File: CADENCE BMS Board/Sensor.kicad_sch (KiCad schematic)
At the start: 65 parts, among them IC1 R5432V407BA, J1 Screw_Terminal_01x02, J21 Conn_01x02, Q1 P-Channel FET, Q10 N-MOS, Q2 60V Enhancement, Q3 60V Enhancement, Q4 60V Enhancement, Q5 Q_NMOS_DSG, Q6 Q_NMOS_DSG, Q7 Q_NMOS_DSG, Q8 N-MOS, Q9 N-MOS, U4 BQ34Z100-R2, U5 MCP9600-E_MX

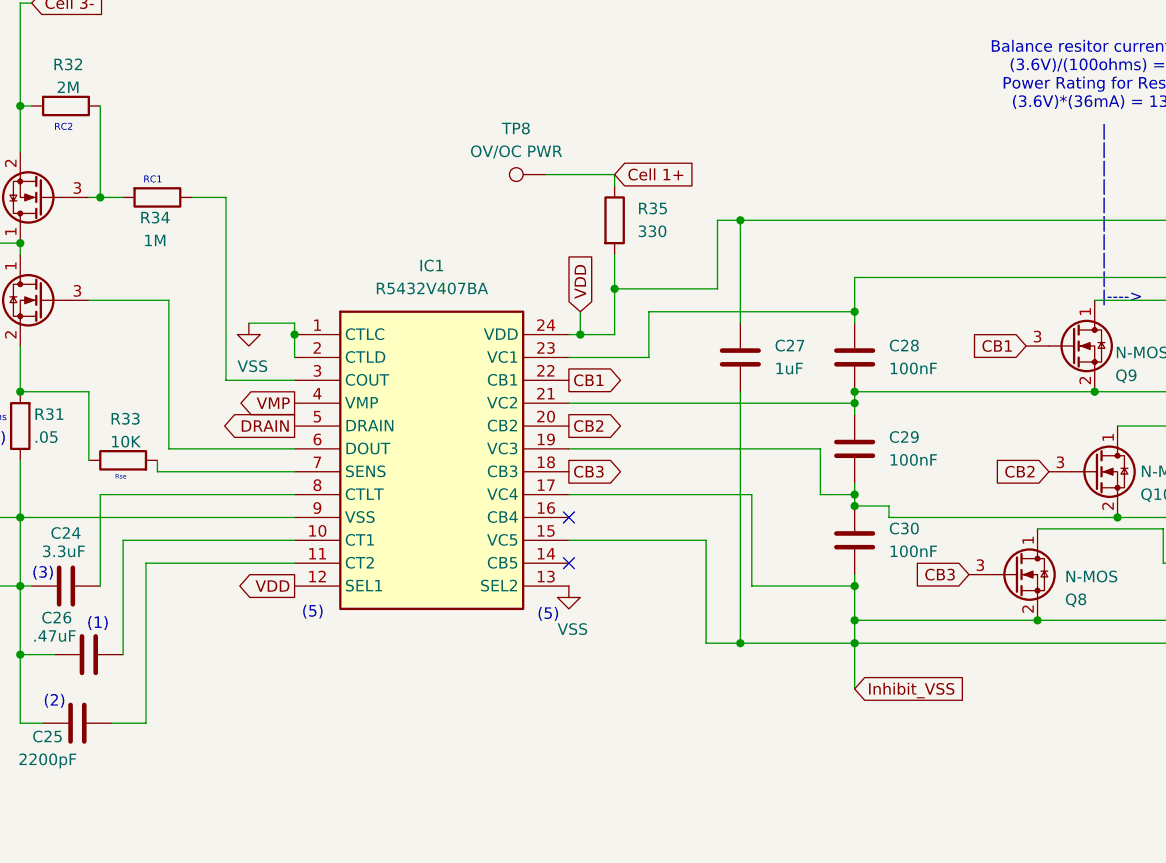
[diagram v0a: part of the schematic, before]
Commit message: Updates to the Inhibit system and Connectors
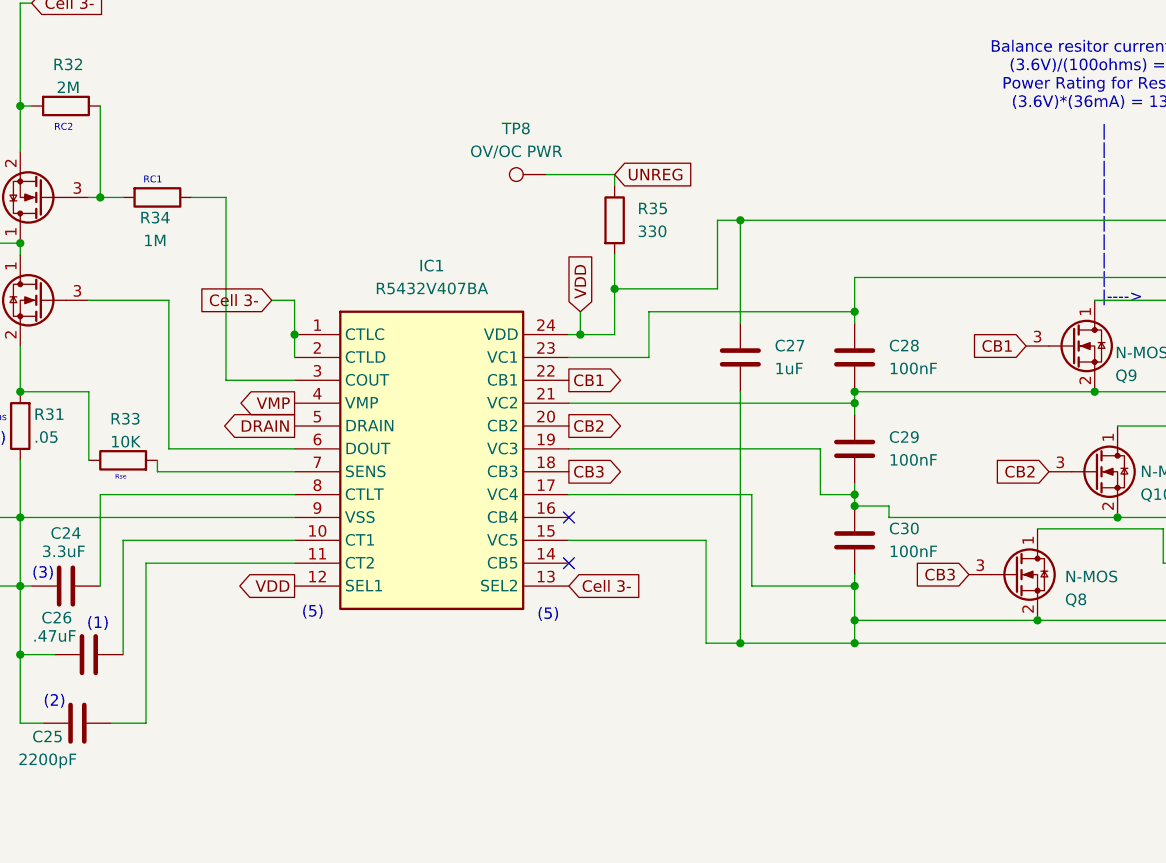
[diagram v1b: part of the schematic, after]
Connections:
- net Cell 1+: no longer R35.1, TP8.1
- net Cell 3-: now also IC1.1 (CTLC), IC1.13 (SEL2), IC1.2 (CTLD)
- net EXP: no longer IC1.1 (CTLC), IC1.13 (SEL2), IC1.2 (CTLD)
- new net UNREG: R35.1, TP8.1
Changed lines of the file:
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@@
 	(wire
 		(pts
-			(xy 397.51 82.55) (xy 397.51 83.82)
+			(xy 397.51 80.01) (xy 397.51 83.82)
 		)
 		(stroke
@@
 	(wire
 		(pts
-			(xy 459.74 118.11) (xy 459.74 123.19)
-		)
-		(stroke
-			(width 0)
-			(type default)
-		)
-	)
-	(wire
-		(pts
 			(xy 189.23 157.48) (xy 182.88 157.48)
 		)
@@
 	(wire
 		(pts
-			(xy 392.43 82.55) (xy 397.51 82.55)
+			(xy 394.97 80.01) (xy 397.51 80.01)
 		)
 		(stroke
@@
 		)
 	)
-	(global_label "Cell 1+"
+	(global_label "UNREG"
 		(shape input)
 		(at 433.07 66.04 0)
@@
 		)
 		(property "Intersheetrefs" "${INTERSHEET_REFS}"
-			(at 443.4937 66.04 0)
+			(at 442.4052 66.04 0)
 			(hide yes)
 			(show_name no)
@@
 		)
 	)
+	(global_label "Cell 3-"
+		(shape input)
+		(at 394.97 80.01 180)
+		(fields_autoplaced yes)
+		(effects
+			(font
+				(size 1.27 1.27)
+			)
+			(justify right)
+		)
+		(property "Intersheetrefs" "${INTERSHEET_REFS}"
+			(at 384.5463 80.01 0)
+			(hide yes)
+			(show_name no)
+			(do_not_autoplace no)
+			(effects
+				(font
+					(size 1.27 1.27)
+				)
+				(justify right)
+			)
+		)
+	)
 	(global_label "CB3"
 		(shape output)
@@
 		)
 	)
-	(global_label "Inhibit_VSS"
-		(shape input)
-		(at 459.74 123.19 0)
-		(fields_autoplaced yes)
-		(effects
-			(font
-				(size 1.27 1.27)
-			)
-			(justify left)
-		)
-		(property "Intersheetrefs" "${INTERSHEET_REFS}"
-			(at 473.1875 123.19 0)
-			(hide yes)
-			(show_name no)
-			(do_not_autoplace no)
-			(effects
-				(font
-					(size 1.27 1.27)
-				)
-				(justify left)
-			)
-		)
-	)
 	(global_label "HS_I2C1_SCL"
 		(shape bidirectional)
@@
 		)
 	)
+	(global_label "Cell 3-"
+		(shape input)
+		(at 427.99 111.76 0)
+		(fields_autoplaced yes)
+		(effects
+			(font
+				(size 1.27 1.27)
+			)
+			(justify left)
+		)
+		(property "Intersheetrefs" "${INTERSHEET_REFS}"
+			(at 438.4137 111.76 0)
+			(hide yes)
+			(show_name no)
+			(do_not_autoplace no)
+			(effects
+				(font
+					(size 1.27 1.27)
+				)
+				(justify left)
+			)
+		)
+	)
 	(global_label "VMP"
 		(shape input)
@@
 	)
 	(symbol
-		(lib_id "power:GND")
-		(at 392.43 82.55 0)
-		(unit 1)
-		(body_style 1)
-		(exclude_from_sim no)
-		(in_bom yes)
-		(on_board yes)
-		(in_pos_files yes)
-		(dnp no)
-		(property "Reference" "#PWR033"
-			(at 392.43 88.9 0)
-			(hide yes)
-			(show_name no)
-			(do_not_autoplace no)
-			(effects
-				(font
-					(size 1.27 1.27)
-				)
-			)
-		)
-		(property "Value" "VSS"
-			(at 391.16 87.376 0)
-			(show_name no)
-			(do_not_autoplace no)
-			(effects
-				(font
-					(size 1.27 1.27)
-				)
-				(justify left)
-			)
-		)
-		(property "Footprint" ""
-			(at 392.43 82.55 0)
-			(hide yes)
-			(show_name no)
-			(do_not_autoplace no)
-			(effects
-				(font
-					(size 1.27 1.27)
-				)
-			)
-		)
-		(property "Datasheet" ""
-			(at 392.43 82.55 0)
-			(hide yes)
-			(show_name no)
-			(do_not_autoplace no)
-			(effects
-				(font
-					(size 1.27 1.27)
-				)
-			)
-		)
-		(property "Description" "Power symbol creates a global label with name \"GND\" , ground"
-			(at 392.43 82.55 0)
-			(hide yes)
-			(show_name no)
-			(do_not_autoplace no)
-			(effects
-				(font
-					(size 1.27 1.27)
-				)
-			)
-		)
-		(pin "1"
-		)
-		(instances
-			(project "BMS_Board_Prototype"
-				(path "/4ee99911-836b-4752-8a2d-327c8b28dc47/3281f8b8-f9b3-4f29-933c-5d0b1d830ef9"
-					(reference "#PWR033")
-					(unit 1)
-				)
-			)
-		)
-	)
-	(symbol
 		(lib_id "Device:R")
 		(at 331.47 127 180)
@@
 					(unit 1)
 				)
-			)
-		)
-	)
-	(symbol
-		(lib_id "power:GND")
-		(at 427.99 111.76 0)
-		(unit 1)
-		(body_style 1)
-		(exclude_from_sim no)
-		(in_bom yes)
-		(on_board yes)
-		(in_pos_files yes)
-		(dnp no)
-		(property "Reference" "#PWR034"
-			(at 427.99 118.11 0)
-			(hide yes)
-			(show_name no)
-			(do_not_autoplace no)
-			(effects
-				(font
-					(size 1.27 1.27)
-				)
-			)
-		)
-		(property "Value" "VSS"
-			(at 426.72 116.586 0)
-			(show_name no)
-			(do_not_autoplace no)
-			(effects
-				(font
-					(size 1.27 1.27)
-				)
-				(justify left)
-			)
-		)
-		(property "Footprint" ""
-			(at 427.99 111.76 0)
-			(hide yes)
-			(show_name no)
-			(do_not_autoplace no)
-			(effects
-				(font
-					(size 1.27 1.27)
-				)
-			)
-		)
-		(property "Datasheet" ""
-			(at 427.99 111.76 0)
-			(hide yes)
-			(show_name no)
-			(do_not_autoplace no)
-			(effects
-				(font
-					(size 1.27 1.27)
-				)
-			)
-		)
-		(property "Description" "Power symbol creates a global label with name \"GND\" , ground"
-			(at 427.99 111.76 0)
-			(hide yes)
-			(show_name no)
-			(do_not_autoplace no)
-			(effects
-				(font
-					(size 1.27 1.27)
-				)
-			)
-		)
-		(pin "1"
-		)
-		(instances
-			(project "BMS_Board_Prototype"
-				(path "/4ee99911-836b-4752-8a2d-327c8b28dc47/3281f8b8-f9b3-4f29-933c-5d0b1d830ef9"
-					(reference "#PWR034")
-					(unit 1)
-				)
